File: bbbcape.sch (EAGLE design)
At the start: 11 parts

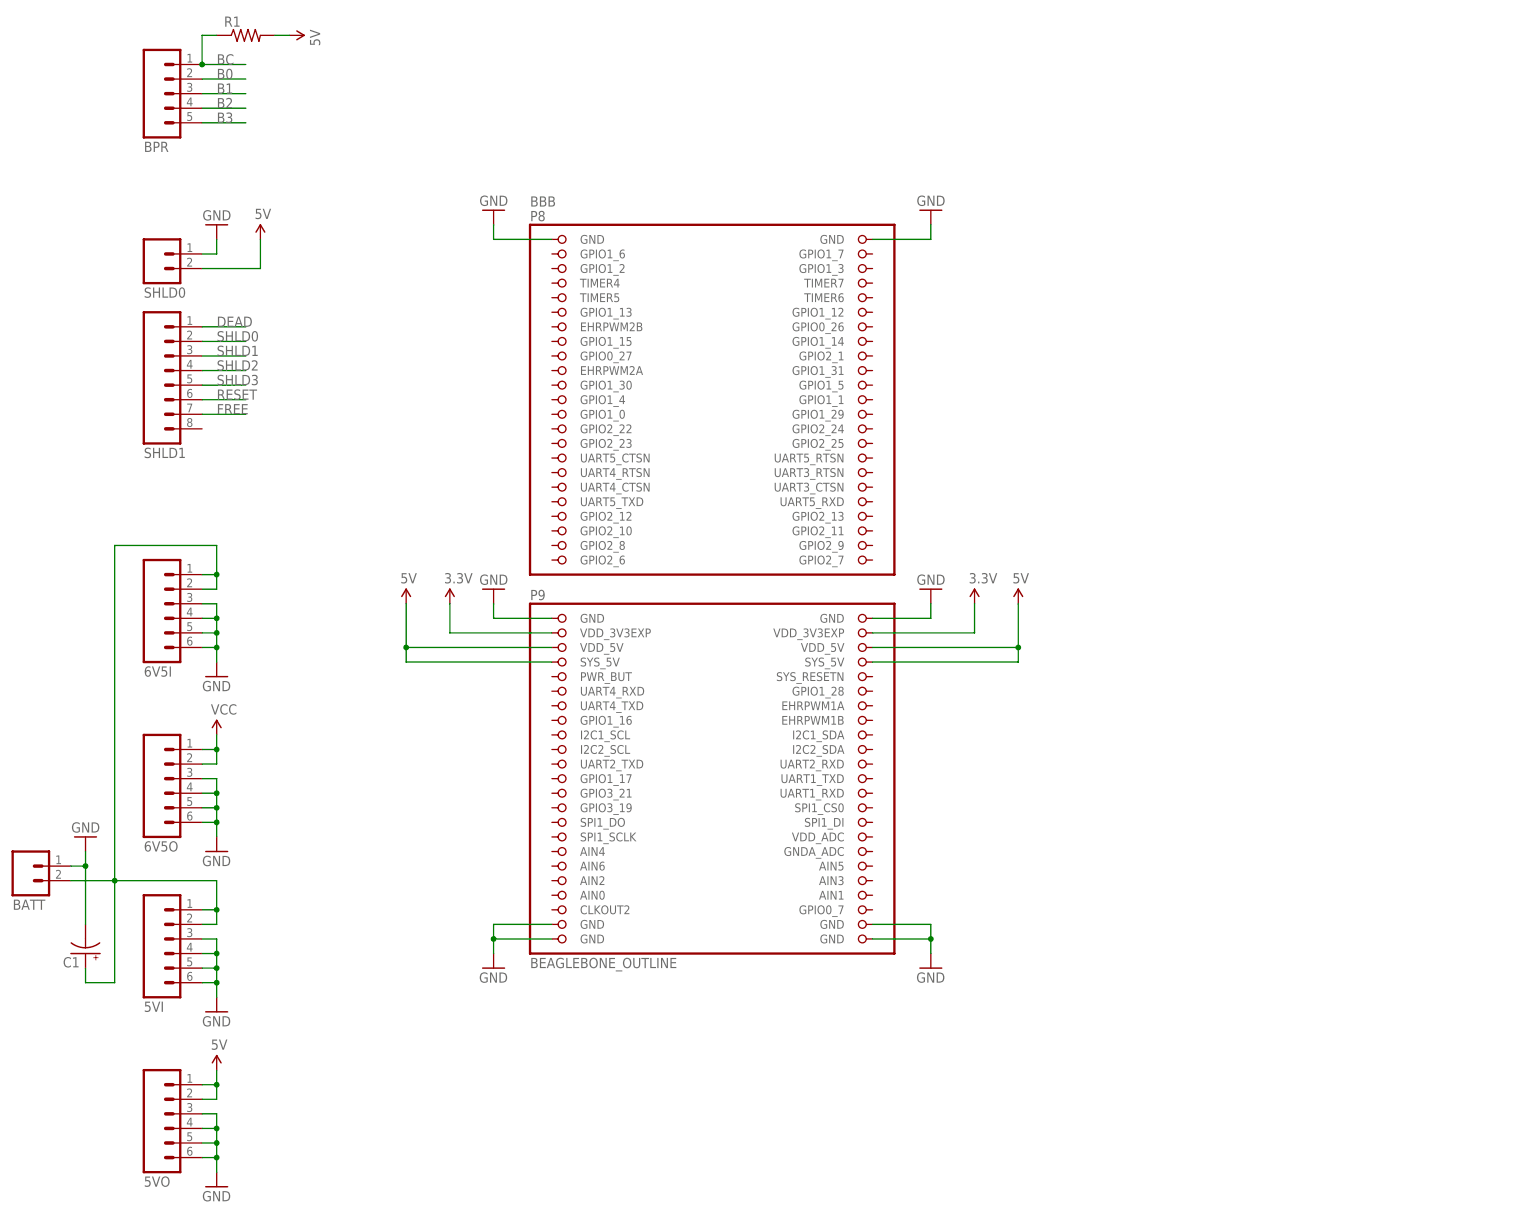
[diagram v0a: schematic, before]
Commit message: Connected motors.
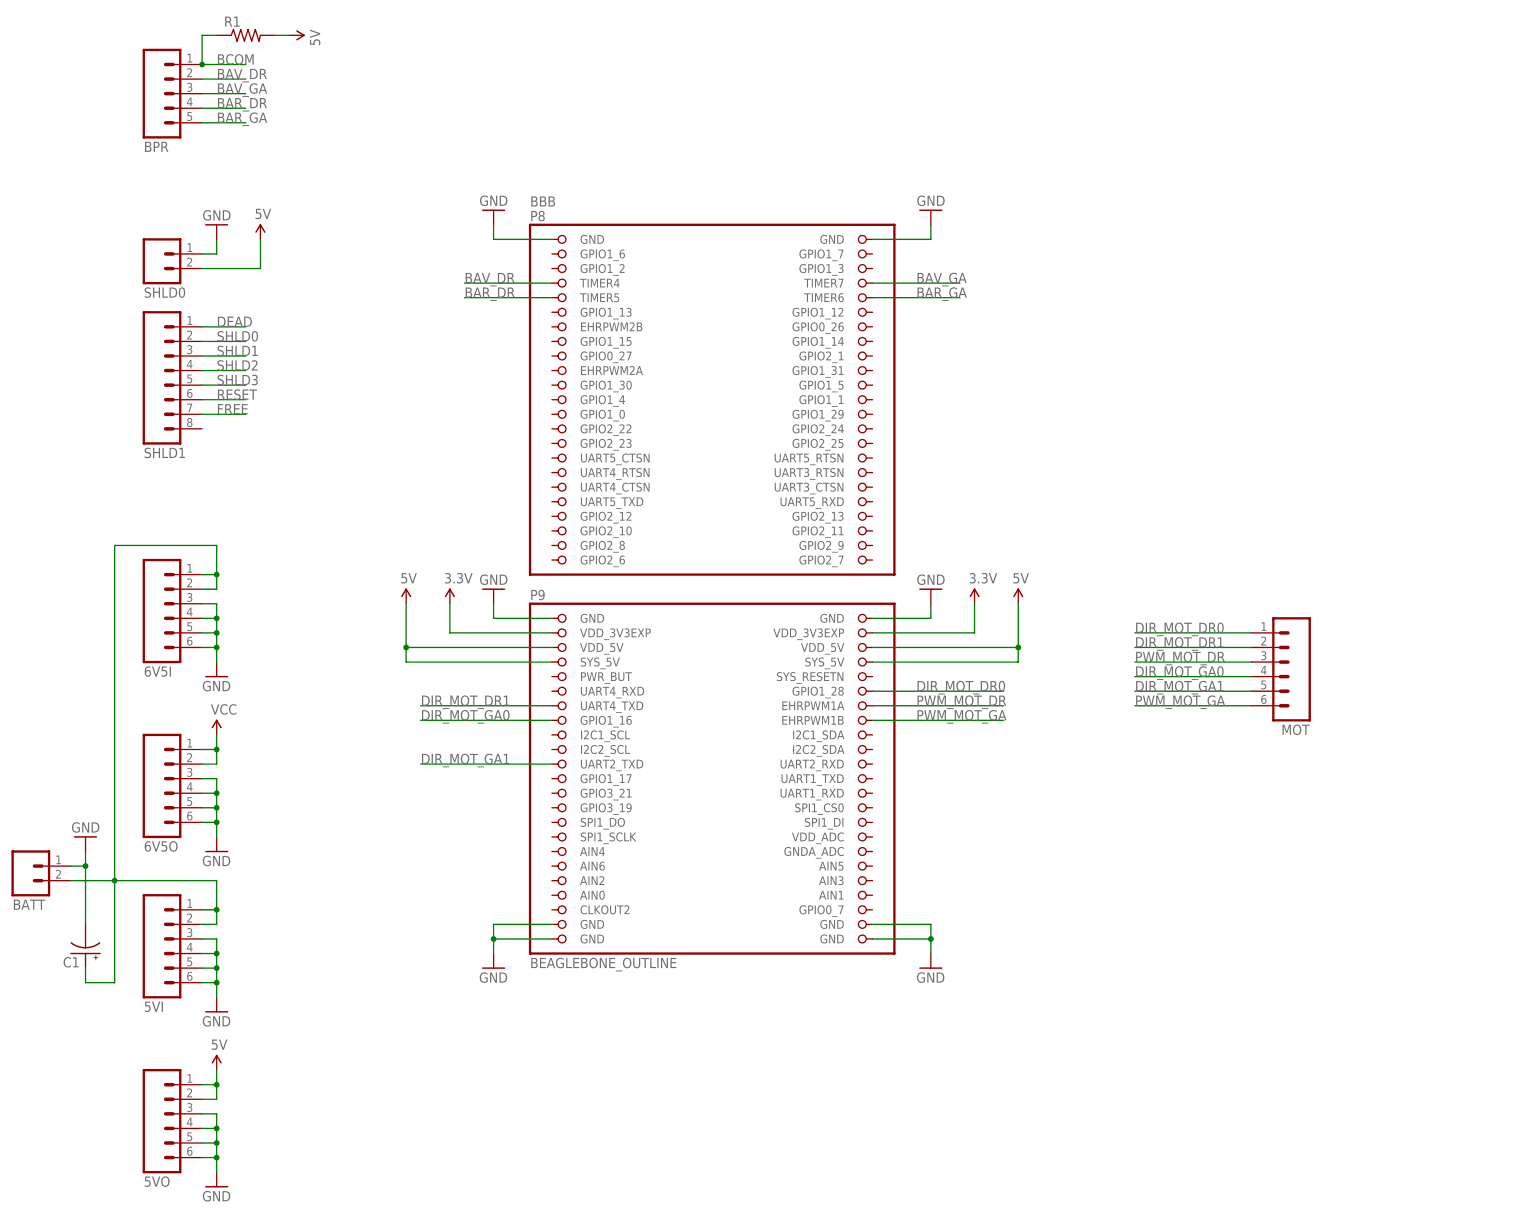
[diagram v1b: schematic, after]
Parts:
- added MOT: (no value), SparkFun-Connectors:M06SILK_FEMALE_PTH
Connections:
- net BC renamed BCOM
- removed net B0: BPR.2
- removed net B1: BPR.3
- removed net B2: BPR.4
- removed net B3: BPR.5
- new net BAR_DR: BBB.TIMER5, BPR.4
- new net BAR_GA: BBB.TIMER6, BPR.5
- new net BAV_DR: BBB.TIMER4, BPR.2
- new net BAV_GA: BBB.TIMER7, BPR.3
- new net DIR_MOT_DR0: BBB.GPIO1_28, MOT.1
- new net DIR_MOT_DR1: BBB.UART4_TXD, MOT.2
- new net DIR_MOT_GA0: BBB.GPIO1_16, MOT.4
- new net DIR_MOT_GA1: BBB.UART2_TXD, MOT.5
- new net PWM_MOT_DR: BBB.EHRPWM1A, MOT.3
- new net PWM_MOT_GA: BBB.EHRPWM1B, MOT.6
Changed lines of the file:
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@@
 <part name="SUPPLY6" library="SparkFun-Aesthetics" deviceset="3.3V" device=""/>
 <part name="SUPPLY7" library="SparkFun-Aesthetics" deviceset="3.3V" device=""/>
+<part name="MOT" library="SparkFun-Connectors" deviceset="M06" device="SILK_FEMALE_PTH"/>
 </parts>
 <sheets>
@@
 <instance part="SUPPLY6" gate="G$1" x="66.04" y="106.68"/>
 <instance part="SUPPLY7" gate="G$1" x="157.48" y="106.68"/>
+<instance part="MOT" gate="G$1" x="210.82" y="96.52" rot="R180"/>
 </instances>
 <busses>
@@
 </segment>
 </net>
-<net name="BC" class="0">
+<net name="BCOM" class="0">
 <segment>
 <pinref part="BPR" gate="G$1" pin="1"/>
@@
 </segment>
 </net>
-<net name="B0" class="0">
+<net name="BAV_DR" class="0">
 <segment>
 <pinref part="BPR" gate="G$1" pin="2"/>
@@
 <label x="25.4" y="198.12" size="1.778" layer="95"/>
 </segment>
-</net>
-<net name="B1" class="0">
+<segment>
+<pinref part="BBB" gate="G$1" pin="TIMER4"/>
+<wire x1="68.58" y1="162.56" x2="83.82" y2="162.56" width="0.1524" layer="91"/>
+<label x="68.58" y="162.56" size="1.778" layer="95"/>
+</segment>
+</net>
+<net name="BAV_GA" class="0">
 <segment>
 <pinref part="BPR" gate="G$1" pin="3"/>
@@
 <label x="25.4" y="195.58" size="1.778" layer="95"/>
 </segment>
-</net>
-<net name="B2" class="0">
+<segment>
+<pinref part="BBB" gate="G$1" pin="TIMER7"/>
+<wire x1="154.94" y1="162.56" x2="139.7" y2="162.56" width="0.1524" layer="91"/>
+<label x="147.32" y="162.56" size="1.778" layer="95"/>
+</segment>
+</net>
+<net name="BAR_DR" class="0">
 <segment>
 <pinref part="BPR" gate="G$1" pin="4"/>
@@
 <label x="25.4" y="193.04" size="1.778" layer="95"/>
 </segment>
-</net>
-<net name="B3" class="0">
+<segment>
+<pinref part="BBB" gate="G$1" pin="TIMER5"/>
+<wire x1="68.58" y1="160.02" x2="83.82" y2="160.02" width="0.1524" layer="91"/>
+<label x="68.58" y="160.02" size="1.778" layer="95"/>
+</segment>
+</net>
+<net name="BAR_GA" class="0">
 <segment>
 <pinref part="BPR" gate="G$1" pin="5"/>
 <wire x1="30.48" y1="190.5" x2="22.86" y2="190.5" width="0.1524" layer="91"/>
 <label x="25.4" y="190.5" size="1.778" layer="95"/>
+</segment>
+<segment>
+<pinref part="BBB" gate="G$1" pin="TIMER6"/>
+<wire x1="154.94" y1="160.02" x2="139.7" y2="160.02" width="0.1524" layer="91"/>
+<label x="147.32" y="160.02" size="1.778" layer="95"/>
 </segment>
 </net>
@@
 </segment>
 </net>
+<net name="DIR_MOT_DR0" class="0">
+<segment>
+<pinref part="BBB" gate="G$1" pin="GPIO1_28"/>
+<wire x1="162.56" y1="91.44" x2="139.7" y2="91.44" width="0.1524" layer="91"/>
+<label x="147.32" y="91.44" size="1.778" layer="95"/>
+</segment>
+<segment>
+<pinref part="MOT" gate="G$1" pin="1"/>
+<wire x1="185.42" y1="101.6" x2="205.74" y2="101.6" width="0.1524" layer="91"/>
+<label x="185.42" y="101.6" size="1.778" layer="95"/>
+</segment>
+</net>
+<net name="PWM_MOT_DR" class="0">
+<segment>
+<pinref part="BBB" gate="G$1" pin="EHRPWM1A"/>
+<wire x1="162.56" y1="88.9" x2="139.7" y2="88.9" width="0.1524" layer="91"/>
+<label x="147.32" y="88.9" size="1.778" layer="95"/>
+</segment>
+<segment>
+<pinref part="MOT" gate="G$1" pin="3"/>
+<wire x1="185.42" y1="96.52" x2="205.74" y2="96.52" width="0.1524" layer="91"/>
+<label x="185.42" y="96.52" size="1.778" layer="95"/>
+</segment>
+</net>
+<net name="PWM_MOT_GA" class="0">
+<segment>
+<pinref part="BBB" gate="G$1" pin="EHRPWM1B"/>
+<wire x1="162.56" y1="86.36" x2="139.7" y2="86.36" width="0.1524" layer="91"/>
+<label x="147.32" y="86.36" size="1.778" layer="95"/>
+</segment>
+<segment>
+<pinref part="MOT" gate="G$1" pin="6"/>
+<wire x1="185.42" y1="88.9" x2="205.74" y2="88.9" width="0.1524" layer="91"/>
+<label x="185.42" y="88.9" size="1.778" layer="95"/>
+</segment>
+</net>
+<net name="DIR_MOT_DR1" class="0">
+<segment>
+<pinref part="BBB" gate="G$1" pin="UART4_TXD"/>
+<wire x1="60.96" y1="88.9" x2="83.82" y2="88.9" width="0.1524" layer="91"/>
+<label x="60.96" y="88.9" size="1.778" layer="95"/>
+</segment>
+<segment>
+<pinref part="MOT" gate="G$1" pin="2"/>
+<wire x1="185.42" y1="99.06" x2="205.74" y2="99.06" width="0.1524" layer="91"/>
+<label x="185.42" y="99.06" size="1.778" layer="95"/>
+</segment>
+</net>
+<net name="DIR_MOT_GA0" class="0">
+<segment>
+<pinref part="BBB" gate="G$1" pin="GPIO1_16"/>
+<wire x1="60.96" y1="86.36" x2="83.82" y2="86.36" width="0.1524" layer="91"/>
+<label x="60.96" y="86.36" size="1.778" layer="95"/>
+</segment>
+<segment>
+<pinref part="MOT" gate="G$1" pin="4"/>
+<wire x1="185.42" y1="93.98" x2="205.74" y2="93.98" width="0.1524" layer="91"/>
+<label x="185.42" y="93.98" size="1.778" layer="95"/>
+</segment>
+</net>
+<net name="DIR_MOT_GA1" class="0">
+<segment>
+<pinref part="BBB" gate="G$1" pin="UART2_TXD"/>
+<wire x1="60.96" y1="78.74" x2="83.82" y2="78.74" width="0.1524" layer="91"/>
+<label x="60.96" y="78.74" size="1.778" layer="95"/>
+</segment>
+<segment>
+<pinref part="MOT" gate="G$1" pin="5"/>
+<wire x1="185.42" y1="91.44" x2="205.74" y2="91.44" width="0.1524" layer="91"/>
+<label x="185.42" y="91.44" size="1.778" layer="95"/>
+</segment>
+</net>

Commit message: Connected CMUCam2+.
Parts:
- added CAM: (no value), SparkFun-Connectors:M06SILK_FEMALE_PTH
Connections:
- new net UART1_RX: BBB.UART1_RXD, CAM.6
- new net UART1_TX: BBB.UART1_TXD, CAM.5
- new net VCC: CAM.2
- net 3.3V: now also CAM.3
- net 5V: now also CAM.4
- net GND: now also CAM.1
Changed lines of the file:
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@@
 <part name="SUPPLY7" library="SparkFun-Aesthetics" deviceset="3.3V" device=""/>
 <part name="MOT" library="SparkFun-Connectors" deviceset="M06" device="SILK_FEMALE_PTH"/>
+<part name="GND13" library="SparkFun-Aesthetics" deviceset="GND" device=""/>
+<part name="CAM" library="SparkFun-Connectors" deviceset="M06" device="SILK_FEMALE_PTH"/>
+<part name="6V1" library="SparkFun-Aesthetics" deviceset="VCC" device=""/>
+<part name="SUPPLY8" library="SparkFun-Aesthetics" deviceset="3.3V" device=""/>
+<part name="SUPPLY9" library="SparkFun-Aesthetics" deviceset="5V" device=""/>
 </parts>
 <sheets>
@@
 <instance part="SUPPLY7" gate="G$1" x="157.48" y="106.68"/>
 <instance part="MOT" gate="G$1" x="210.82" y="96.52" rot="R180"/>
+<instance part="GND13" gate="1" x="203.2" y="78.74" rot="R180"/>
+<instance part="CAM" gate="G$1" x="210.82" y="68.58" rot="R180"/>
+<instance part="6V1" gate="G$1" x="195.58" y="76.2"/>
+<instance part="SUPPLY8" gate="G$1" x="187.96" y="76.2"/>
+<instance part="SUPPLY9" gate="G$1" x="180.34" y="76.2"/>
 </instances>
 <busses>
@@
 <wire x1="22.86" y1="10.16" x2="25.4" y2="10.16" width="0.1524" layer="91"/>
 <junction x="25.4" y="10.16"/>
+</segment>
+<segment>
+<pinref part="GND13" gate="1" pin="GND"/>
+<wire x1="203.2" y1="76.2" x2="203.2" y2="73.66" width="0.1524" layer="91"/>
+<wire x1="203.2" y1="73.66" x2="205.74" y2="73.66" width="0.1524" layer="91"/>
+<pinref part="CAM" gate="G$1" pin="1"/>
 </segment>
 </net>
@@
 <junction x="165.1" y="99.06"/>
 </segment>
+<segment>
+<pinref part="SUPPLY9" gate="G$1" pin="5V"/>
+<wire x1="180.34" y1="76.2" x2="180.34" y2="66.04" width="0.1524" layer="91"/>
+<pinref part="CAM" gate="G$1" pin="4"/>
+<wire x1="180.34" y1="66.04" x2="205.74" y2="66.04" width="0.1524" layer="91"/>
+<label x="198.12" y="66.04" size="1.778" layer="95"/>
+</segment>
 </net>
 <net name="DEAD" class="0">
@@
 <wire x1="157.48" y1="101.6" x2="157.48" y2="106.68" width="0.1524" layer="91"/>
 </segment>
+<segment>
+<pinref part="SUPPLY8" gate="G$1" pin="3.3V"/>
+<wire x1="187.96" y1="76.2" x2="187.96" y2="68.58" width="0.1524" layer="91"/>
+<pinref part="CAM" gate="G$1" pin="3"/>
+<wire x1="187.96" y1="68.58" x2="205.74" y2="68.58" width="0.1524" layer="91"/>
+<label x="198.12" y="68.58" size="1.778" layer="95"/>
+</segment>
 </net>
 <net name="DIR_MOT_DR0" class="0">
@@
 </segment>
 </net>
+<net name="VCC" class="0">
+<segment>
+<pinref part="6V1" gate="G$1" pin="VCC"/>
+<wire x1="195.58" y1="76.2" x2="195.58" y2="71.12" width="0.1524" layer="91"/>
+<pinref part="CAM" gate="G$1" pin="2"/>
+<wire x1="195.58" y1="71.12" x2="205.74" y2="71.12" width="0.1524" layer="91"/>
+<label x="198.12" y="71.12" size="1.778" layer="95"/>
+</segment>
+</net>
+<net name="UART1_TX" class="0">
+<segment>
+<pinref part="BBB" gate="G$1" pin="UART1_TXD"/>
+<wire x1="157.48" y1="76.2" x2="139.7" y2="76.2" width="0.1524" layer="91"/>
+<label x="147.32" y="76.2" size="1.778" layer="95"/>
+</segment>
+<segment>
+<pinref part="CAM" gate="G$1" pin="5"/>
+<wire x1="193.04" y1="63.5" x2="205.74" y2="63.5" width="0.1524" layer="91"/>
+<label x="193.04" y="63.5" size="1.778" layer="95"/>
+</segment>
+</net>
+<net name="UART1_RX" class="0">
+<segment>
+<pinref part="BBB" gate="G$1" pin="UART1_RXD"/>
+<wire x1="157.48" y1="73.66" x2="139.7" y2="73.66" width="0.1524" layer="91"/>
+<label x="147.32" y="73.66" size="1.778" layer="95"/>
+</segment>
+<segment>
+<pinref part="CAM" gate="G$1" pin="6"/>
+<wire x1="193.04" y1="60.96" x2="205.74" y2="60.96" width="0.1524" layer="91"/>
+<label x="193.04" y="60.96" size="1.778" layer="95"/>
+</segment>
+</net>

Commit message: Connected bumpers.
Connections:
- net BCOM: now also BBB.GPIO1_12
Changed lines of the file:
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@@
 <wire x1="22.86" y1="205.74" x2="25.4" y2="205.74" width="0.1524" layer="91"/>
+</segment>
+<segment>
+<pinref part="BBB" gate="G$1" pin="GPIO1_12"/>
+<wire x1="154.94" y1="157.48" x2="139.7" y2="157.48" width="0.1524" layer="91"/>
+<label x="147.32" y="157.48" size="1.778" layer="95"/>
 </segment>
 </net>

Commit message: Added frame.
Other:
- note added: "Author: Michel Lavoie"
- note added: "Date: 2016-12-11"
- note added: "Project: Marcus"
- note added: "Revision : 0.1.0"
- note added: "Title: BBB cape for my robot"
- moved on the sheet: 5VI, 5VO, 6V5I, 6V5O, BATT, BBB, BPR, C1, CAM, MOT, R1, SHLD0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
